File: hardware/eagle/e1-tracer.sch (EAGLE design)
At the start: 118 parts, among them IC1 MCP1703T-1202E/CB, IC2 W25Q80DVSNIG, IC3 TLV70233DBVR, IC4 ASEM1-12.000MHZ-LC-T, J1 PASSTHROUGH, M1 MENTOR_12701001, M2 MENTOR_12701001, SW1 TACTSW-TL3340, T1 BC847C, T2 BC847C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

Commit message: e1-tracer: Add various BOM attributes
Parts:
- C25: MANUFACTURERPARTNUMBER UNKNOWN MANUFACTURER PART NUMBER -> 399-4696-1-ND
- CDONE: SOURCEPARTNUMBER UNKNOWN SOURCE PART NUMBER -> 160-1827-1-ND
- IC3: LINK UNKNOWN LINK -> https://www.digikey.de/product-detail/de/texas-instruments/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; SOURCEPARTNUMBER UNKNOWN SOURCE PART NUMBER -> 296-32415-1-ND
- L2, L3: LINK UNKNOWN LINK -> https://www.digikey.de/product-detail/de/bourns-inc/CE20121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; SOURCEPARTNUMBER UNKNOWN SOURCE PART NUMBER -> CE201210-47NJCT-ND
- PWR: SOURCEPARTNUMBER UNKNOWN SOURCE PART NUMBER -> 511-1645-1-ND
- R1: LINK UNKNOWN LINK -> https://www.digikey.de/product-detail/de/stackpole-electron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; SOURCEPARTNUMBER UNKNOWN SOURCE PART NUMBER -> RMCF0603JT100RCT-ND
- R10: DESCRIPTION RES 10K OHM 1%% 1/10W 0603 -> NO DESCRIPTION; LINK https://www.digikey.de/product-detail/de/stackpole-electronics-inc/RMCF0603FT10K0/RMCF0603FT10K0CT-ND -> https://www.digikey.de/product-detail/de/stackpole-electronics-inc/RMCF0603JT10K0/RMCF0603JT10K0CT-ND; MANUFACTURER Stackpole Electronics Inc -> UNKNOWN MANUFACTURER; MANUFACTURERPARTNUMBER RMCF0603FT10K0 -> UNKNOWN MANUFACTURER PART NUMBER; SOURCE DIGIKEY -> UNKNOWN SOURCE; SOURCEPARTNUMBER RMCF0603FT10K0CT-ND -> RMCF0603JT10K0CT-ND
- R13, R8: DESCRIPTION RES 10K OHM 1%% 1/10W 0603 -> NO DESCRIPTION; LINK https://www.digikey.de/product-detail/de/stackpole-electronics-inc/RMCF0603FT10K0/RMCF0603FT10K0CT-ND -> https://www.digikey.de/product-detail/de/stackpole-electronics-inc/RMCF0603JT10K0/RMCF0603JT10K0CT-ND; MANUFACTURER Stackpole Electronics Inc -> UNKNOWN MANUFACTURER; MANUFACTURERPARTNUMBER YPE HTML PUBLIC -> UNKNOWN MANUFACTURER PART NUMBER; ROHSCERTIFICATE Bleifrei / RoHS3-konform -> UNKNOWN ROHS CERTIFICATE; SOURCE DIGIKEY -> UNKNOWN SOURCE; SOURCEPARTNUMBER RMCF0603FT10K0CT-ND -> RMCF0603JT10K0CT-ND
- R14: LINK UNKNOWN LINK -> https://www.digikey.de/product-detail/de/stackpole-electron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; SOURCEPARTNUMBER UNKNOWN SOURCE PART NUMBER -> RMCF0603JT2K20CT-ND
- R16, R17, R18, R19, R20, R21, R22, R23, R24, R25, R26, R27, R28, R29, R30, R31, R32, R33, R36, R37: LINK UNKNOWN LINK -> https://www.digikey.de/product-detail/de/stackpole-electron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; SOURCEPARTNUMBER UNKNOWN SOURCE PART NUMBER -> RMCF0603JT10K0CT-ND
- R34, R35: LINK UNKNOWN LINK -> https://www.digikey.de/product-detail/de/stackpole-electron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; SOURCE UNKNOWN SOURCE -> RMCF0603FT3K00CT-ND
- R38, R39: LINK UNKNOWN LINK -> https://www.digikey.de/product-detail/de/stackpole-electron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; SOURCEPARTNUMBER UNKNOWN SOURCE PART NUMBER -> RMCF0603JT120RCT-ND
- R42, R43: LINK UNKNOWN LINK -> https://www.digikey.de/product-detail/de/stackpole-electron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; SOURCE UNKNOWN SOURCE -> RMCF0603JT1K00CT-ND
- R6, R7: LINK UNKNOWN LINK -> https://www.digikey.de/product-detail/de/stackpole-electron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; SOURCEPARTNUMBER UNKNOWN SOURCE PART NUMBER -> RMCF0603JT33R0CT-ND
- R9: LINK UNKNOWN LINK -> https://www.digikey.de/product-detail/de/stackpole-electron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; SOURCEPARTNUMBER UNKNOWN SOURCE PART NUMBER -> RMCF0603JT1K50CT-ND
- U4: LINK UNKNOWN LINK -> https://www.digikey.de/product-detail/de/renesas-electronic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; SOURCEPARTNUMBER UNKNOWN SOURCE PART NUMBER -> 800-2347-ND
- U6: LINK UNKNOWN LINK -> https://www.digikey.de/product-detail/de/renesas-electronic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; SOURCEPARTNUMBER UNKNOWN SOURCE PART NUMBER -> 631-1182-ND

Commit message: e1-tracer: collect more BOM atrributes
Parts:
- C25: DESCRIPTION NO DESCRIPTION -> CAP CER 22UF 6.3V X5R 0805; MANUFACTURER UNKNOWN MANUFACTURER -> KEMET; MANUFACTURERPARTNUMBER 399-4696-1-ND -> C0805C226M9PACTU; SOURCE UNKNOWN SOURCE -> DIGIKEY; SOURCEPARTNUMBER UNKNOWN SOURCE PART NUMBER -> 399-4696-1-ND
- C26, C27, C28: DESCRIPTION NO DESCRIPTION -> CAP CER 22UF 6.3V X5R 0805; MANUFACTURER UNKNOWN MANUFACTURER -> KEMET; MANUFACTURERPARTNUMBER UNKNOWN MANUFACTURER PART NUMBER -> C0805C226M9PACTU; SOURCE UNKNOWN SOURCE -> DIGIKEY; SOURCEPARTNUMBER UNKNOWN SOURCE PART NUMBER -> 399-4696-1-ND
- CDONE: DESCRIPTION NO DESCRIPTION -> LED BLUE CLEAR CHIP SMD; MANUFACTURER UNKNOWN MANUFACTURER -> Lite-On Inc.; MANUFACTURERPARTNUMBER UNKNOWN MANUFACTURER PART NUMBER -> LTST-C193TBKT-5A; SOURCE UNKNOWN SOURCE -> DIGIKEY
- IC3: DESCRIPTION NO DESCRIPTION -> IC REG LINEAR 3.3V 300MA SOT23-5; MANUFACTURER UNKNOWN MANUFACTURER -> Texas Instruments; MANUFACTURERPARTNUMBER UNKNOWN MANUFACTURER PART NUMBER -> TLV70233DBVR; SOURCE UNKNOWN SOURCE -> DIGIKEY
- J1: DESCRIPTION NO DESCRIPTION -> CONN MOD JACK 8P8C R/A UNSHLD; MANUFACTURER UNKNOWN MANUFACTURER -> TE Connectivity AMP Connectors; MANUFACTURERPARTNUMBER UNKNOWN MANUFACTURER PART NUMBER -> 5557560-1; SOURCE UNKNOWN SOURCE -> DIGIKEY
- L2, L3: DESCRIPTION NO DESCRIPTION -> FIXED IND 47NH 300MA 700MOHM SMD; MANUFACTURER UNKNOWN MANUFACTURER -> Bourns Inc.; MANUFACTURERPARTNUMBER UNKNOWN MANUFACTURER PART NUMBER -> CE201210-47NJ; SOURCE UNKNOWN SOURCE -> DIGIKEY
- PWR: DESCRIPTION NO DESCRIPTION -> LED GREEN CLEAR 2PLCC SMD; MANUFACTURER UNKNOWN MANUFACTURER -> Rohm Semiconductor; MANUFACTURERPARTNUMBER UNKNOWN MANUFACTURER PART NUMBER -> SML-Z14PTT86A; SOURCE UNKNOWN SOURCE -> DIGIKEY
- R1: DESCRIPTION NO DESCRIPTION -> RES 100 OHM 5%% 1/10W 0603; MANUFACTURER UNKNOWN MANUFACTURER -> Stackpole Electronics Inc; MANUFACTURERPARTNUMBER UNKNOWN MANUFACTURER PART NUMBER -> RMCF0603JT100R; SOURCE UNKNOWN SOURCE -> DIGIKEY
- R10, R13, R16, R17, R18, R19, R20, R21, R22, R23, R24, R25, R26, R27, R28, R29, R30, R31, R32, R33, R36, R37, R8: DESCRIPTION NO DESCRIPTION -> RES 10K OHM 5%% 1/10W 0603; MANUFACTURER UNKNOWN MANUFACTURER -> Stackpole Electronics Inc; MANUFACTURERPARTNUMBER UNKNOWN MANUFACTURER PART NUMBER -> RMCF0603JT10K0; SOURCE UNKNOWN SOURCE -> DIGIKEY
- R14: DESCRIPTION NO DESCRIPTION -> RES 2.2K OHM 5%% 1/10W 0603; MANUFACTURER UNKNOWN MANUFACTURER -> Stackpole Electronics Inc; MANUFACTURERPARTNUMBER UNKNOWN MANUFACTURER PART NUMBER -> RMCF0603JT2K20; SOURCE UNKNOWN SOURCE -> DIGIKEY
- R34, R35: DESCRIPTION NO DESCRIPTION -> RES 3K OHM 1%% 1/10W 0603; MANUFACTURER UNKNOWN MANUFACTURER -> Stackpole Electronics Inc; MANUFACTURERPARTNUMBER UNKNOWN MANUFACTURER PART NUMBER -> RMCF0603FT3K00; SOURCE RMCF0603FT3K00CT-ND -> DIGIKEY; SOURCEPARTNUMBER UNKNOWN SOURCE PART NUMBER -> RMCF0603FT3K00CT-ND
- R38, R39: DESCRIPTION NO DESCRIPTION -> RES 120 OHM 5%% 1/10W 0603; MANUFACTURER UNKNOWN MANUFACTURER -> Stackpole Electronics Inc; MANUFACTURERPARTNUMBER UNKNOWN MANUFACTURER PART NUMBER -> RMCF0603JT120R; SOURCE UNKNOWN SOURCE -> DIGIKEY
- R42, R43: DESCRIPTION NO DESCRIPTION -> RES 1K OHM 5%% 1/10W 0603; MANUFACTURER UNKNOWN MANUFACTURER -> Stackpole Electronics Inc; MANUFACTURERPARTNUMBER UNKNOWN MANUFACTURER PART NUMBER -> RMCF0603JT1K00; SOURCE RMCF0603JT1K00CT-ND -> DIGIKEY; SOURCEPARTNUMBER UNKNOWN SOURCE PART NUMBER -> RMCF0603JT1K00CT-ND
- R6, R7: DESCRIPTION NO DESCRIPTION -> RES 33 OHM 5%% 1/10W 0603; MANUFACTURER UNKNOWN MANUFACTURER -> Stackpole Electronics Inc; MANUFACTURERPARTNUMBER UNKNOWN MANUFACTURER PART NUMBER -> RMCF0603JT33R0; SOURCE UNKNOWN SOURCE -> DIGIKEY
- R9: DESCRIPTION NO DESCRIPTION -> RES 1.5K OHM 5%% 1/10W 0603; MANUFACTURER UNKNOWN MANUFACTURER -> Stackpole Electronics Inc; MANUFACTURERPARTNUMBER UNKNOWN MANUFACTURER PART NUMBER -> RMCF0603JT1K50; SOURCE UNKNOWN SOURCE -> DIGIKEY; SOURCEPARTNUMBER RMCF0603JT1K50CT-ND -> RMCF0603JT1K50CT-ND
- U4: DESCRIPTION NO DESCRIPTION -> IC TELECOM INTERFACE 44TQFP; MANUFACTURER UNKNOWN MANUFACTURER -> Renesas Electronics America Inc.; MANUFACTURERPARTNUMBER UNKNOWN MANUFACTURER PART NUMBER -> 82V2081PPG; SOURCE UNKNOWN SOURCE -> DIGIKEY
- U6: DESCRIPTION NO DESCRIPTION -> XTAL OSC XO 2.0480MHZ HCMOS SMD; MANUFACTURER UNKNOWN MANUFACTURER -> Renesas Electronics America Inc.; SOURCE UNKNOWN SOURCE -> DIGIKEY

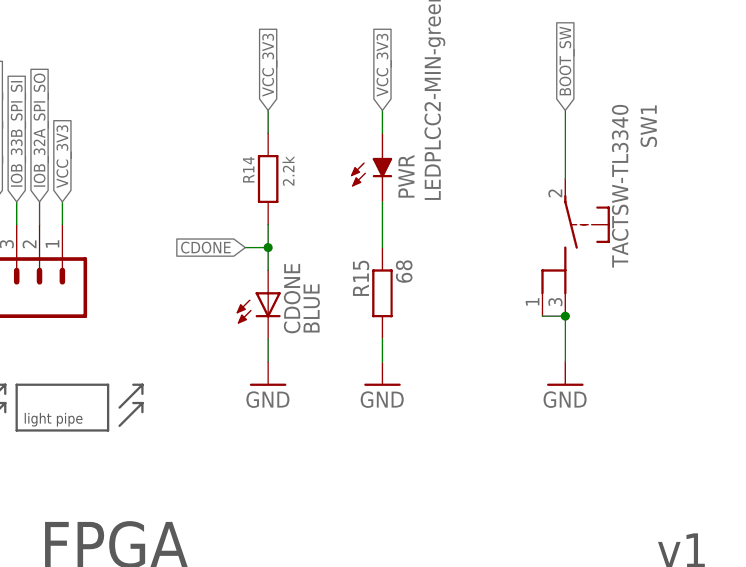
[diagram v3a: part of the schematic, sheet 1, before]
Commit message: e1-tracer: more eBOM atrributes + commit eBOM
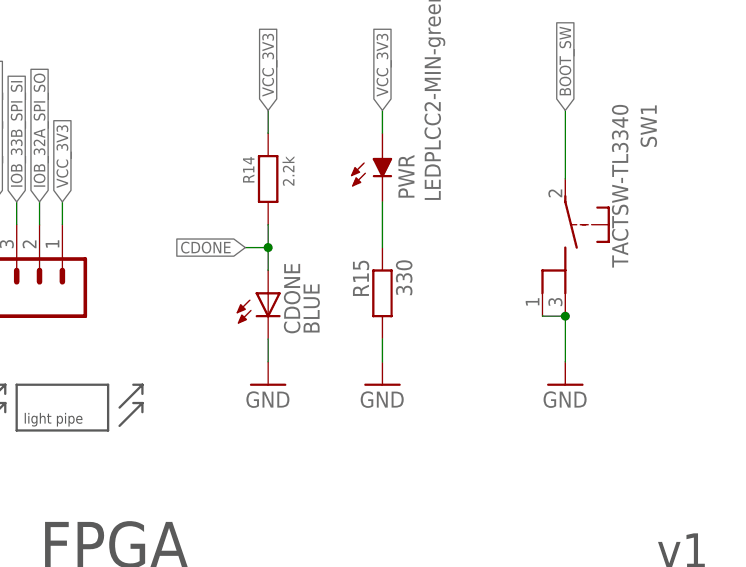
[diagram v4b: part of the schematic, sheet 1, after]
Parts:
- CDONE: CLASS UNKNOWN CLASS -> LED
- IC1, IC2, IC3: CLASS UNKNOWN CLASS -> IC
- IC4: CLASS UNKNOWN CLASS -> IC / XTAL / XO
- M1, M2: CLASS UNKNOWN CLASS -> LIGHT GUIDE; MANUFACTURERPARTNUMBER UNKNOWN MANUFACTURER PART NUMBER -> 1270.1001
- R15: value 68 -> 330; DESCRIPTION NO DESCRIPTION -> RES SMD 330 OHM 1%% 1/10W 0603; LINK UNKNOWN LINK -> https://www.digikey.de/product-detail/de/yageo/RC0603FR-073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; MANUFACTURER UNKNOWN MANUFACTURER -> Yageo; MANUFACTURERPARTNUMBER UNKNOWN MANUFACTURER PART NUMBER -> RC0603FR-07330RL; SOURCE UNKNOWN SOURCE -> DIGIKEY; SOURCEPARTNUMBER UNKNOWN SOURCE PART NUMBER -> 311-330HRCT-ND
- SW1: CLASS UNKNOWN CLASS -> SWITCH
- T1, T2: CLASS UNKNOWN CLASS -> TRANSISTOR; DESCRIPTION NO DESCRIPTION -> TRANS NPN 45V 0.1A SOT23; LINK UNKNOWN LINK -> https://www.digikey.de/product-detail/de/nexperia-usa-inc/B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; MANUFACTURER UNKNOWN MANUFACTURER -> Nexperia USA Inc.; MANUFACTURERPARTNUMBER UNKNOWN MANUFACTURER PART NUMBER -> BC847C,215; SOURCE UNKNOWN SOURCE -> DIGIKEY; SOURCEPARTNUMBER UNKNOWN SOURCE PART NUMBER -> 1727-2924-1-ND
- U5: DESCRIPTION NO DESCRIPTION -> IC TELECOM INTERFACE 44TQFP; LINK UNKNOWN LINK -> https://www.digikey.de/product-detail/de/renesas-electronic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; MANUFACTURER UNKNOWN MANUFACTURER -> Renesas Electronics America Inc.; MANUFACTURERPARTNUMBER UNKNOWN MANUFACTURER PART NUMBER -> 82V2081PPG; SOURCE UNKNOWN SOURCE -> DIGIKEY; SOURCEPARTNUMBER UNKNOWN SOURCE PART NUMBER -> 800-2347-ND
- U6: CLASS IC -> IC / XTAL / XO
- U7: CLASS IC -> IC / XTAL / XO; POPULATED TRUE -> FALSE

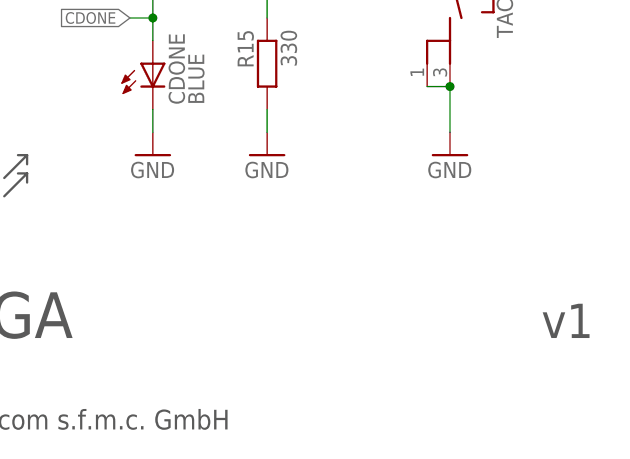
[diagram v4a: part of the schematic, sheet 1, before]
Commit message: e1-tracer: denote CC-BY-SA 4.0 in schema (adds to SYS#5052)
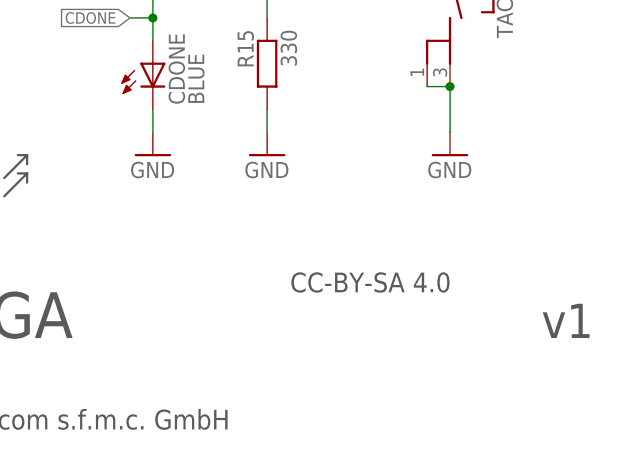
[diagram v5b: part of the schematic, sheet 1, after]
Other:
- note added: "CC-BY-SA 4.0"
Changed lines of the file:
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@@
 <grid distance="0.1" unitdist="inch" unit="inch" style="lines" multiple="1" display="no" altdistance="0.01" altunitdist="inch" altunit="inch"/>
 <layers>
-<layer number="1" name="Top" color="4" fill="1" visible="yes" active="no"/>
-<layer number="2" name="Route2" color="1" fill="3" visible="yes" active="no"/>
-<layer number="3" name="Route3" color="4" fill="3" visible="yes" active="no"/>
-<layer number="4" name="Route4" color="1" fill="4" visible="yes" active="no"/>
-<layer number="5" name="Route5" color="4" fill="4" visible="yes" active="no"/>
-<layer number="6" name="Route6" color="1" fill="8" visible="yes" active="no"/>
-<layer number="7" name="Route7" color="4" fill="8" visible="yes" active="no"/>
-<layer number="8" name="Route8" color="1" fill="2" visible="yes" active="no"/>
-<layer number="9" name="Route9" color="4" fill="2" visible="yes" active="no"/>
-<layer number="10" name="Route10" color="1" fill="7" visible="yes" active="no"/>
-<layer number="11" name="Route11" color="4" fill="7" visible="yes" active="no"/>
-<layer number="12" name="Route12" color="1" fill="5" visible="yes" active="no"/>
-<layer number="13" name="Route13" color="4" fill="5" visible="yes" active="no"/>
-<layer number="14" name="Route14" color="1" fill="6" visible="yes" active="no"/>
-<layer number="15" name="Route15" color="4" fill="6" visible="yes" active="no"/>
-<layer number="16" name="Bottom" color="1" fill="1" visible="yes" active="no"/>
-<layer number="17" name="Pads" color="2" fill="1" visible="yes" active="no"/>
-<layer number="18" name="Vias" color="2" fill="1" visible="yes" active="no"/>
-<layer number="19" name="Unrouted" color="6" fill="1" visible="yes" active="no"/>
-<layer number="20" name="Dimension" color="15" fill="1" visible="yes" active="no"/>
-<layer number="21" name="tPlace" color="7" fill="1" visible="yes" active="no"/>
-<layer number="22" name="bPlace" color="7" fill="1" visible="yes" active="no"/>
-<layer number="23" name="tOrigins" color="15" fill="1" visible="yes" active="no"/>
-<layer number="24" name="bOrigins" color="15" fill="1" visible="yes" active="no"/>
-<layer number="25" name="tNames" color="7" fill="1" visible="yes" active="no"/>
-<layer number="26" name="bNames" color="7" fill="1" visible="yes" active="no"/>
-<layer number="27" name="tValues" color="7" fill="1" visible="yes" active="no"/>
-<layer number="28" name="bValues" color="7" fill="1" visible="yes" active="no"/>
+<layer number="1" name="Top" color="4" fill="1" visible="no" active="no"/>
+<layer number="2" name="Route2" color="1" fill="3" visible="no" active="no"/>
+<layer number="3" name="Route3" color="4" fill="3" visible="no" active="no"/>
+<layer number="4" name="Route4" color="1" fill="4" visible="no" active="no"/>
+<layer number="5" name="Route5" color="4" fill="4" visible="no" active="no"/>
+<layer number="6" name="Route6" color="1" fill="8" visible="no" active="no"/>
+<layer number="7" name="Route7" color="4" fill="8" visible="no" active="no"/>
+<layer number="8" name="Route8" color="1" fill="2" visible="no" active="no"/>
+<layer number="9" name="Route9" color="4" fill="2" visible="no" active="no"/>
+<layer number="10" name="Route10" color="1" fill="7" visible="no" active="no"/>
+<layer number="11" name="Route11" color="4" fill="7" visible="no" active="no"/>
+<layer number="12" name="Route12" color="1" fill="5" visible="no" active="no"/>
+<layer number="13" name="Route13" color="4" fill="5" visible="no" active="no"/>
+<layer number="14" name="Route14" color="1" fill="6" visible="no" active="no"/>
+<layer number="15" name="Route15" color="4" fill="6" visible="no" active="no"/>
+<layer number="16" name="Bottom" color="1" fill="1" visible="no" active="no"/>
+<layer number="17" name="Pads" color="2" fill="1" visible="no" active="no"/>
+<layer number="18" name="Vias" color="2" fill="1" visible="no" active="no"/>
+<layer number="19" name="Unrouted" color="6" fill="1" visible="no" active="no"/>
+<layer number="20" name="Dimension" color="15" fill="1" visible="no" active="no"/>
+<layer number="21" name="tPlace" color="7" fill="1" visible="no" active="no"/>
+<layer number="22" name="bPlace" color="7" fill="1" visible="no" active="no"/>
+<layer number="23" name="tOrigins" color="15" fill="1" visible="no" active="no"/>
+<layer number="24" name="bOrigins" color="15" fill="1" visible="no" active="no"/>
+<layer number="25" name="tNames" color="7" fill="1" visible="no" active="no"/>
+<layer number="26" name="bNames" color="7" fill="1" visible="no" active="no"/>
+<layer number="27" name="tValues" color="7" fill="1" visible="no" active="no"/>
+<layer number="28" name="bValues" color="7" fill="1" visible="no" active="no"/>
 <layer number="29" name="tStop" color="7" fill="3" visible="no" active="no"/>
 <layer number="30" name="bStop" color="7" fill="6" visible="no" active="no"/>
@@
 <layer number="35" name="tGlue" color="7" fill="4" visible="no" active="no"/>
 <layer number="36" name="bGlue" color="7" fill="5" visible="no" active="no"/>
-<layer number="37" name="tTest" color="7" fill="1" visible="yes" active="no"/>
-<layer number="38" name="bTest" color="7" fill="1" visible="yes" active="no"/>
+<layer number="37" name="tTest" color="7" fill="1" visible="no" active="no"/>
+<layer number="38" name="bTest" color="7" fill="1" visible="no" active="no"/>
 <layer number="39" name="tKeepout" color="4" fill="11" visible="no" active="no"/>
 <layer number="40" name="bKeepout" color="1" fill="11" visible="no" active="no"/>
@@
 <layer number="44" name="Drills" color="7" fill="1" visible="no" active="no"/>
 <layer number="45" name="Holes" color="7" fill="1" visible="no" active="no"/>
-<layer number="46" name="Milling" color="3" fill="1" visible="yes" active="no"/>
-<layer number="47" name="Measures" color="7" fill="1" visible="yes" active="no"/>
-<layer number="48" name="Document" color="7" fill="1" visible="yes" active="no"/>
-<layer number="49" name="Reference" color="7" fill="1" visible="yes" active="no"/>
-<layer number="50" name="dxf" color="7" fill="1" visible="yes" active="no"/>
-<layer number="51" name="tDocu" color="7" fill="1" visible="yes" active="no"/>
-<layer number="52" name="bDocu" color="7" fill="1" visible="yes" active="no"/>
-<layer number="53" name="tGND_GNDA" color="7" fill="9" visible="yes" active="no"/>
-<layer number="54" name="bGND_GNDA" color="1" fill="9" visible="yes" active="no"/>
-<layer number="56" name="wert" color="7" fill="1" visible="yes" active="no"/>
-<layer number="57" name="tCAD" color="6" fill="1" visible="yes" active="no"/>
-<layer number="59" name="tMark" color="7" fill="1" visible="yes" active="no"/>
-<layer number="60" name="bMark" color="7" fill="1" visible="yes" active="no"/>
+<layer number="46" name="Milling" color="3" fill="1" visible="no" active="no"/>
+<layer number="47" name="Measures" color="7" fill="1" visible="no" active="no"/>
+<layer number="48" name="Document" color="7" fill="1" visible="no" active="no"/>
+<layer number="49" name="Reference" color="7" fill="1" visible="no" active="no"/>
+<layer number="50" name="dxf" color="7" fill="1" visible="no" active="no"/>
+<layer number="51" name="tDocu" color="7" fill="1" visible="no" active="no"/>
+<layer number="52" name="bDocu" color="7" fill="1" visible="no" active="no"/>
+<layer number="53" name="tGND_GNDA" color="7" fill="9" visible="no" active="no"/>
+<layer number="54" name="bGND_GNDA" color="1" fill="9" visible="no" active="no"/>
+<layer number="56" name="wert" color="7" fill="1" visible="no" active="no"/>
+<layer number="57" name="tCAD" color="6" fill="1" visible="no" active="no"/>
+<layer number="59" name="tMark" color="7" fill="1" visible="no" active="no"/>
+<layer number="60" name="bMark" color="7" fill="1" visible="no" active="no"/>
 <layer number="88" name="SimResults" color="9" fill="1" visible="yes" active="yes"/>
 <layer number="89" name="SimProbes" color="9" fill="1" visible="yes" active="yes"/>
@@
 <wire x1="292.1" y1="177.8" x2="292.1" y2="101.6" width="0.1524" layer="97" style="longdash"/>
 <wire x1="271.78" y1="91.44" x2="271.78" y2="10.16" width="0.1524" layer="97" style="longdash"/>
+<text x="345.44" y="20.32" size="2.1844" layer="97">CC-BY-SA 4.0</text>
 </plain>
 <instances>
@@
 <text x="373.38" y="15.24" size="3.81" layer="97">&gt;REVISION</text>
 <text x="292.1" y="5.08" size="2.1844" layer="97">(c) 2020 sysmocom s.f.m.c. GmbH</text>
+<text x="345.44" y="20.32" size="2.1844" layer="97">CC-BY-SA 4.0</text>
 </plain>
 <instances>
